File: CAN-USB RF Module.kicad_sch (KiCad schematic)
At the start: 27 parts, among them J1 Conn_01x05_Pin, J2 USB_B_Micro, J3 Conn_Coaxial, SW1 RESET, SW2 BOOT0, U1 STM32L562CETx, U2 TLV2217-33KVURG3, U3 AT86RF215-ZU, U4 MCP2542WFDxMF, Y1 8 MHz

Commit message: Added most parts still have to pick better power regulator
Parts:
- removed C3, C4: 100n, symbol Device:C
- removed J1: Conn_01x05_Pin, Connector_PinHeader_2.54mm:PinHeader_1x05_P2.54mm_Vertical, symbol Connector:Conn_01x05_Pin
- removed U1: STM32L562CETx, Package_QFP:LQFP-48_7x7mm_P0.5mm, symbol MCU_ST_STM32L5:STM32L562CETx
- removed U3: AT86RF215-ZU, footprints:QFN48_7X7_PQ_MCH, symbol 2023-05-29_04-56-52:AT86RF215-ZU
- added C14: 100n, Capacitor_SMD:C_0402_1005Metric, symbol Device:C
- added C15: 100u, Capacitor_SMD:C_0402_1005Metric, symbol Device:C
- added CR1: ESDCAN03-2BWY, SOT323-3L_STM, symbol RF_Parts:ESDCAN03-2BWY
- added D2: USBLC6-2SC6, digikey-footprints:SOT23-6L, symbol dk_TVS-Diodes:USBLC6-2SC6
- added D3: ESDA7P120-1U1M, ESDA8P801U1M, symbol RF_Parts:ESDA7P120-1U1M
- added D4: SMLVT3V3, DIOM5436X265N, symbol RF_Parts:SMLVT3V3
- added IC1: ESDALC6V1W5, SOT65P210X110-5N, symbol RF_Parts:ESDALC6V1W5
- added J1, J4: Conn_01x06_Pin, Connector_PinHeader_2.54mm:PinHeader_1x06_P2.54mm_Vertical, symbol Connector:Conn_01x06_Pin
- added R3: 390, Resistor_SMD:R_0402_1005Metric, symbol Device:R
- added U1: STM32L442KCUx, Package_DFN_QFN:QFN-32-1EP_5x5mm_P0.5mm_EP3.45x3.45mm, symbol MCU_ST_STM32L4:STM32L442KCUx
- added U3: SX1280IMLTRT, QFN24_4X4_SEM, symbol RF_Parts:SX1280IMLTRT
- C1, C10, C11, C2, C7, C8: footprint (none) -> Capacitor_SMD:C_0402_1005Metric
- C12, C13: value 100n -> 14p; footprint (none) -> Capacitor_SMD:C_0402_1005Metric
- C5, C6, C9: footprint (none) -> Capacitor_SMD:C_0603_1608Metric
- D1: footprint (none) -> LED_SMD:LED_0402_1005Metric
- FB1: footprint (none) -> Resistor_SMD:R_0603_1608Metric
- J2: footprint Connector_USB:USB_Micro-B_Amphenol_10104110_Horizontal -> footprints:1981568-1
- R1: footprint (none) -> Resistor_SMD:R_0402_1005Metric
- R2: footprint (none) -> Resistor_SMD:R_0805_2012Metric
- SW1: footprint (none) -> footprints:SMD_025816_WRE
- SW2: footprint (none) -> Button_Switch_SMD:SW_SPDT_PCM12
- U2: footprint footprints:KVU3_TEX -> KVU3_TEX; symbol 2023-05-29_05-41-45:TLV2217-33KVURG3 -> RF_Parts:TLV2217-33KVURG3
- U4: value MCP2542WFDxMF -> MCP2542WFDxMF (CAN)
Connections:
- net +3.3V: now also U4.3 (VDD), C15.2, D4.1 (K), J4.1 (Pin_1), U1.1 (VDD), U1.17 (VDD)
- net +3.3VA: now also U1.5 (VDDA)
- net BOOT0: now also U1.31 (PH3)
- net GND: now also U4.2 (VSS), U4.9 (VSS), C14.1, C15.1, CR1.3, D2.2, D3.2 (A), D4.2 (A), IC1.2 (GND), J1.6 (Pin_6), J4.3 (Pin_3), U1.16 (VSS), U1.32 (VSS), U1.33 (VSS)
- net NRST: now also IC1.1 (I/01), J4.5 (Pin_5), U1.4 (NRST)
- net RCC_OSC_OUT: now also R3.2; no longer C12.1, Y1.4
- net VBUS: now also J2.4 (ID), C14.2, D2.5, D3.1 (K)
- net USART2_CANTX: now reaches U4.1 (TXD)
- net USART2_CANTX: now also U1.20 (PA10)
- net USART2_CANRX: now reaches U4.4 (RXD)
- net USART2_CANRX: now also U1.19 (PA9)
- net at U4.6 (CANL): now also CR1.1, J1.4 (Pin_4)
- net at U4.7 (CANH): now also CR1.2, J1.2 (Pin_2)
- net USART2_CANSTBY: now reaches U4.8 (STBY)
- net USART2_CANSTBY: now also U1.18 (PA8)
- net USB_D-_C: now reaches J2.2 (D-)
- net USB_D-_C: now also D2.1
- net USB_D+_C: now reaches J2.3 (D+)
- net USB_D+_C: now also D2.3
- new net: C12.1, R3.1, Y1.4
- new net DEBUG_JTDO-SWO: IC1.3 (I/02), J4.6 (Pin_6)
- new net DEBUG_JTSK_SWCLK: IC1.5 (I/04), J4.2 (Pin_2), U1.24 (PA14)
- new net DEBUG_JTSK_SWDIO: IC1.4 (I/03), J4.4 (Pin_4), U1.23 (PA13)
- new net DEBUG_JTSK_SWO: U1.26 (PB3)
- new net USB_D+: D2.4, U1.22 (PA12)
- new net USB_D-: D2.6, U1.21 (PA11)
- no-connect marks 0 -> 21
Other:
- note added: "(CL - CS) * 2 = C1,2 = (12p - 5p) * 2 = 14p"
- note added: "8MHz External Crystal HSE"
- note added: "ESD Protected CAN Tranciever"
- note added: "ESD Protected USB"
- note added: "STLINK Debug Connector with ESD Protection"
- note added: "STM32L442KCUx"
- note added: "USB Power 5v and CAN Power 12v to 3v3 With ESD Protection"
- note removed: "STM32L562CET6"
- note removed: "USB Power 5v and CAN Power 12v to 3v3"
- moved on the sheet: C1, C10, C11, C12, C13, C2, C5, C6, C7, C8, D1, FB1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

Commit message: l
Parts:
- added H1, H2, H4: MountingHole, symbol Mechanical:MountingHole
- added H3: MountingHole, MountingHole:MountingHole_2.2mm_M2_DIN965, symbol Mechanical:MountingHole
- added U5: MCP2517FD-xSL, Package_SO:SOIC-14_3.9x8.7mm_P1.27mm, symbol Interface_CAN_LIN:MCP2517FD-xSL
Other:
- note added: "Talks over UART not SPI"
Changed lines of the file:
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@@
     (effects (font (size 1.27 1.27)) (justify left bottom))
   )
-  (text "Final parts bill:\n\nLDO Voltage Regulator : https://www.digikey.ca/en/products/detail/texas-instruments/TLV2217-33KVURG3/1096010\n\nSTM32L562CET6 : https://www.st.com/en/microcontrollers-microprocessors/stm32l562ce.html#sample-buy\n\nRF Tranciever AT86RF215-ZU : https://www.digikey.ca/en/products/detail/microchip-technology/AT86RF215-ZU/5147177\n\nCAN Tranciever MCP2544WFD-E/FSN : https://www.digikey.ca/en/products/detail/microchip-technology/MCP2544WFD-E%2FSN/5975771\n\n8 MHz Crystal Occilator ECS-80-12-33-JGN-TR : https://www.digikey.ca/en/products/detail/ecs-inc/ECS-80-12-33-JGN-TR/10478754\n\nUSB ESD PROTECTION TVS : https://www.digikey.ca/en/products/detail/stmicroelectronics/USBLC6-2SC6/1040559\n\nSWD ESD PROTECTION IC : https://www.digikey.ca/en/products/detail/stmicroelectronics/ESDALC6V1W5/1037997\n\nSWD ESD PROTECTION DIODE : https://www.digikey.ca/en/products/detail/stmicroelectronics/SMLVT3V3/603521\n\nPOWER DIODE ESDA7P120-1U1M : https://www.digikey.ca/en/products/detail/stmicroelectronics/ESDA7P120-1U1M/6709858\n\nCAN Transciever ESD Protection ESDCAN03-2BWY : https://www.digikey.ca/en/products/detail/stmicroelectronics/ESDCAN03-2BWY/5305266\n\nButton Push : https://www.digikey.ca/en/products/detail/w%C3%BCrth-elektronik/434133025816/9950810\n\n"
-    (at 444.5 77.47 0)
+  (text "Final parts bill:\n\nLDO Voltage Regulator : https://www.digikey.ca/en/products/detail/texas-instruments/TLV2217-33KVURG3/1096010\n\nSTM32L562CET6 : https://www.st.com/en/microcontrollers-microprocessors/stm32l562ce.html#sample-buy\n\nRF Tranciever AT86RF215-ZU : https://www.digikey.ca/en/products/detail/microchip-technology/AT86RF215-ZU/5147177\n\nCAN Tranciever MCP2544WFD-E/FSN : https://www.digikey.ca/en/products/detail/microchip-technology/MCP2544WFD-E%2FSN/5975771\n\n8 MHz Crystal Occilator ECS-80-12-33-JGN-TR : https://www.digikey.ca/en/products/detail/ecs-inc/ECS-80-12-33-JGN-TR/10478754\n\nUSB ESD PROTECTION TVS : https://www.digikey.ca/en/products/detail/stmicroelectronics/USBLC6-2SC6/1040559\n\nSWD ESD PROTECTION IC : https://www.digikey.ca/en/products/detail/stmicroelectronics/ESDALC6V1W5/1037997\n\nSWD ESD PROTECTION DIODE : https://www.digikey.ca/en/products/detail/stmicroelectronics/SMLVT3V3/603521\n\nPOWER DIODE ESDA7P120-1U1M : https://www.digikey.ca/en/products/detail/stmicroelectronics/ESDA7P120-1U1M/6709858\n\nCAN Transciever ESD Protection ESDCAN03-2BWY : https://www.digikey.ca/en/products/detail/stmicroelectronics/ESDCAN03-2BWY/5305266\n\nButton Push : https://www.digikey.ca/en/products/detail/w%C3%BCrth-elektronik/434133025816/9950810\n\nCAN 2.0 Controller MCP2517FD-H/FSL : https://www.digikey.ca/en/products/detail/microchip-technology/MCP2517FD-H%2FSL/7691348?"
+    (at 444.5 86.36 0)
     (effects (font (size 1.27 1.27)) (justify left bottom))
   )
@@
   )
   (text "ESD Protected CAN Tranciever\n" (at 289.56 236.855 0)
+    (effects (font (size 1.27 1.27)) (justify left bottom))
+  )
+  (text "Talks over UART not SPI\n" (at 33.02 146.05 0)
     (effects (font (size 1.27 1.27)) (justify left bottom))
   )
@@
         (path "/05ffaa46-4df3-4c93-a015-882eb69d3f55"
           (reference "C7") (unit 1)
+        )
+      )
+    )
+  )
+  (symbol (lib_id "Mechanical:MountingHole") (at 32.385 81.28 0) (unit 1)
+    (in_bom yes) (on_board yes) (dnp no) (fields_autoplaced)
+    (property "Reference" "H1" (at 35.56 80.645 0)
+      (effects (font (size 1.27 1.27)) (justify left))
+    )
+    (property "Value" "MountingHole" (at 35.56 83.185 0)
+      (effects (font (size 1.27 1.27)) (justify left))
+    )
+    (property "Footprint" "" (at 32.385 81.28 0)
+      (effects (font (size 1.27 1.27)) hide)
+    )
+    (property "Datasheet" "~" (at 32.385 81.28 0)
+      (effects (font (size 1.27 1.27)) hide)
+    )
+    (instances
+      (project "CAN-USB RF Module"
+        (path "/05ffaa46-4df3-4c93-a015-882eb69d3f55"
+          (reference "H1") (unit 1)
         )
       )
@@
     )
   )
+  (symbol (lib_id "Mechanical:MountingHole") (at 41.91 81.28 0) (unit 1)
+    (in_bom yes) (on_board yes) (dnp no) (fields_autoplaced)
+    (property "Reference" "H2" (at 45.085 80.645 0)
+      (effects (font (size 1.27 1.27)) (justify left))
+    )
+    (property "Value" "MountingHole" (at 45.085 83.185 0)
+      (effects (font (size 1.27 1.27)) (justify left))
+    )
+    (property "Footprint" "" (at 41.91 81.28 0)
+      (effects (font (size 1.27 1.27)) hide)
+    )
+    (property "Datasheet" "~" (at 41.91 81.28 0)
+      (effects (font (size 1.27 1.27)) hide)
+    )
+    (instances
+      (project "CAN-USB RF Module"
+        (path "/05ffaa46-4df3-4c93-a015-882eb69d3f55"
+          (reference "H2") (unit 1)
+        )
+      )
+    )
+  )
   (symbol (lib_id "power:GND") (at 469.265 117.475 0) (unit 1)
     (in_bom yes) (on_board yes) (dnp no) (fields_autoplaced)
@@
     )
   )
+  (symbol (lib_id "Mechanical:MountingHole") (at 51.435 81.915 0) (unit 1)
+    (in_bom yes) (on_board yes) (dnp no) (fields_autoplaced)
+    (property "Reference" "H3" (at 54.61 81.28 0)
+      (effects (font (size 1.27 1.27)) (justify left))
+    )
+    (property "Value" "MountingHole" (at 54.61 83.82 0)
+      (effects (font (size 1.27 1.27)) (justify left))
+    )
+    (property "Footprint" "MountingHole:MountingHole_2.2mm_M2_DIN965" (at 51.435 81.915 0)
+      (effects (font (size 1.27 1.27)) hide)
+    )
+    (property "Datasheet" "~" (at 51.435 81.915 0)
+      (effects (font (size 1.27 1.27)) hide)
+    )
+    (instances
+      (project "CAN-USB RF Module"
+        (path "/05ffaa46-4df3-4c93-a015-882eb69d3f55"
+          (reference "H3") (unit 1)
+        )
+      )
+    )
+  )
   (symbol (lib_id "Device:C") (at 194.945 36.195 0) (unit 1)
     (in_bom yes) (on_board yes) (dnp no)
@@
         (path "/05ffaa46-4df3-4c93-a015-882eb69d3f55"
           (reference "C5") (unit 1)
+        )
+      )
+    )
+  )
+  (symbol (lib_id "Mechanical:MountingHole") (at 61.595 81.915 0) (unit 1)
+    (in_bom yes) (on_board yes) (dnp no) (fields_autoplaced)
+    (property "Reference" "H4" (at 64.77 81.28 0)
+      (effects (font (size 1.27 1.27)) (justify left))
+    )
+    (property "Value" "MountingHole" (at 64.77 83.82 0)
+      (effects (font (size 1.27 1.27)) (justify left))
+    )
+    (property "Footprint" "" (at 61.595 81.915 0)
+      (effects (font (size 1.27 1.27)) hide)
+    )
+    (property "Datasheet" "~" (at 61.595 81.915 0)
+      (effects (font (size 1.27 1.27)) hide)
+    )
+    (instances
+      (project "CAN-USB RF Module"
+        (path "/05ffaa46-4df3-4c93-a015-882eb69d3f55"
+          (reference "H4") (unit 1)
         )
       )
@@
         )
       )
+    )
+  )
+  (symbol (lib_id "Interface_CAN_LIN:MCP2517FD-xSL") (at 367.665 217.805 0) (unit 1)
+    (in_bom yes) (on_board yes) (dnp no) (fields_autoplaced)
+    (property "Reference" "U5" (at 369.6209 203.835 0)
+      (effects (font (size 1.27 1.27)) (justify left))
+    )
+    (property "Value" "MCP2517FD-xSL" (at 369.6209 206.375 0)
+      (effects (font (size 1.27 1.27)) (justify left))
+    )
+    (property "Footprint" "Package_SO:SOIC-14_3.9x8.7mm_P1.27mm" (at 367.665 243.205 0)
+      (effects (font (size 1.27 1.27)) hide)
+    )
+    (property "Datasheet" "https://ww1.microchip.com/downloads/en/DeviceDoc/20005688A.pdf" (at 367.665 211.455 0)
+      (effects (font (size 1.27 1.27)) hide)
+    )
+    (pin "1")
+    (pin "10")
+    (pin "11")
+    (pin "12")
+    (pin "13")
+    (pin "14")
+    (pin "2")
+    (pin "3")
+    (pin "4")
+    (pin "5")
+    (pin "6")
+    (pin "7")
+    (pin "8")
+    (pin "9")
+    (instances
+      (project "CAN-USB RF Module"
+        (path "/05ffaa46-4df3-4c93-a015-882eb69d3f55"
+          (reference "U5") (unit 1)
+        )
+      )

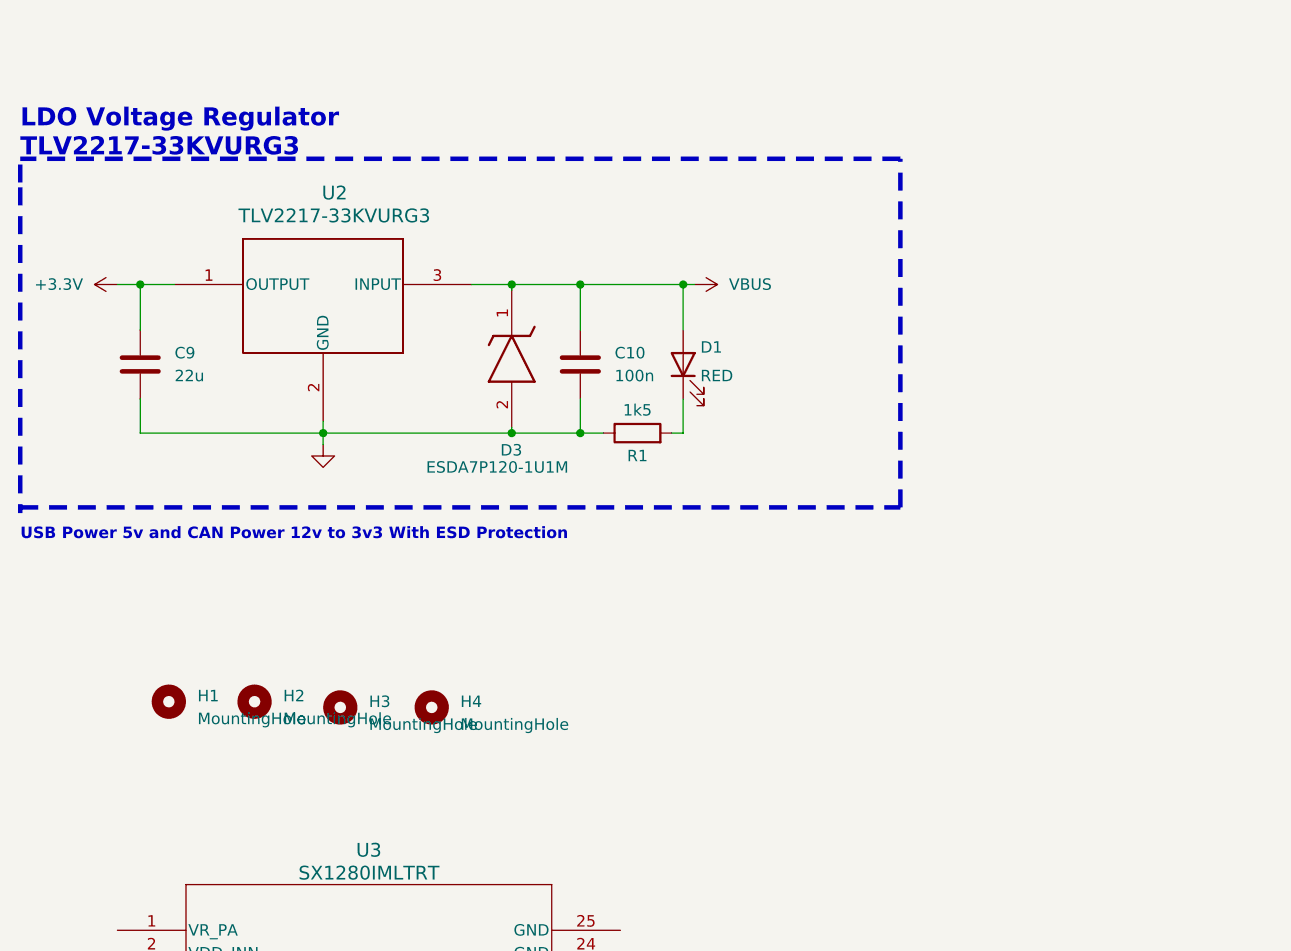
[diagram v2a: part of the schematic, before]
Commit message: Added Sheet for power regulator
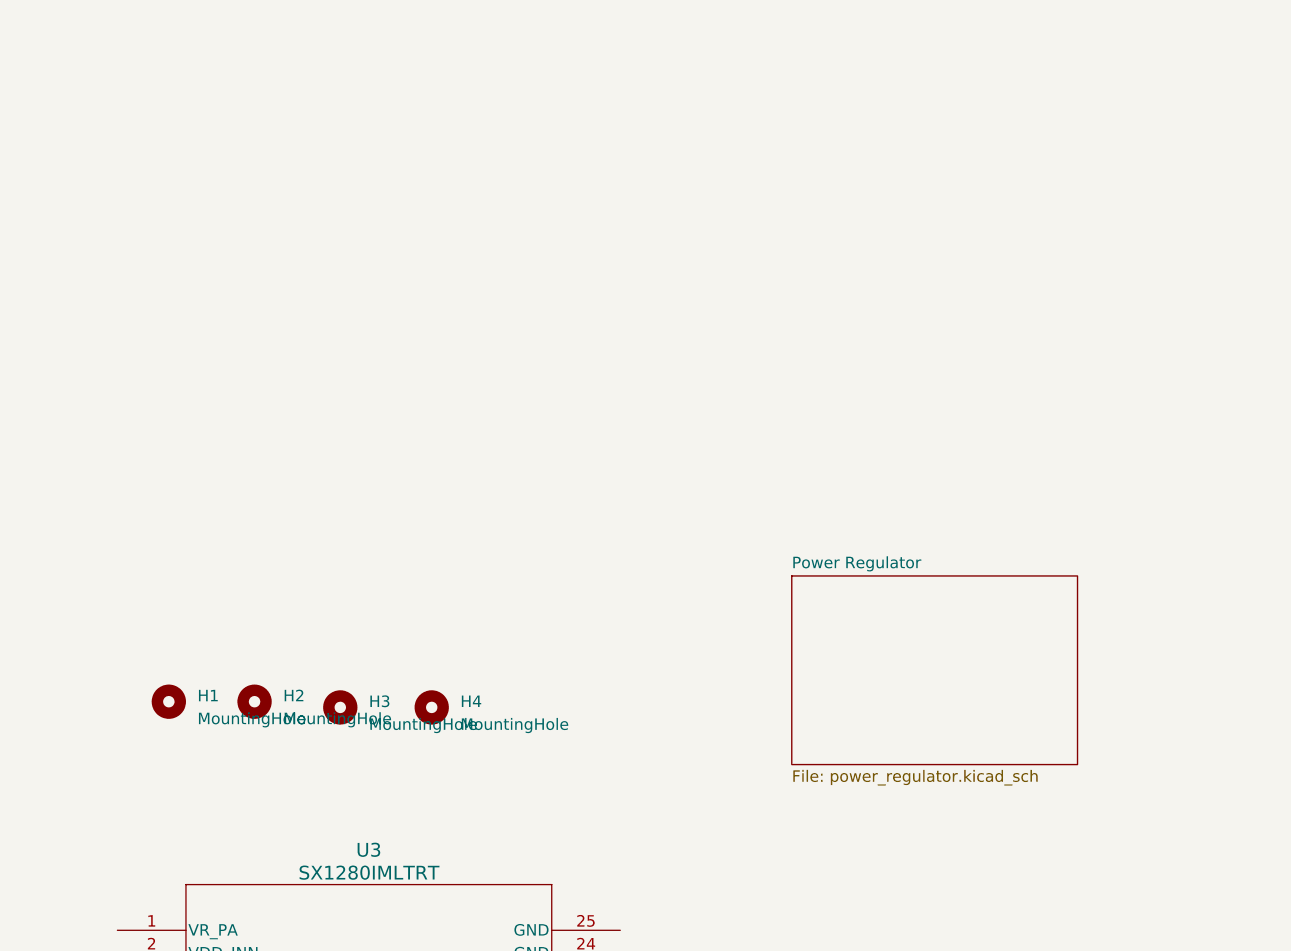
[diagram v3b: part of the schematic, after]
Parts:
- removed C10: 100n, Capacitor_SMD:C_0402_1005Metric, symbol Device:C
- removed C9: 22u, Capacitor_SMD:C_0603_1608Metric, symbol Device:C
- removed D1: RED, LED_SMD:LED_0402_1005Metric, symbol Device:LED
- removed D3: ESDA7P120-1U1M, ESDA8P801U1M, symbol RF_Parts:ESDA7P120-1U1M
- removed R1: 1k5, Resistor_SMD:R_0402_1005Metric, symbol Device:R
- removed U2: TLV2217-33KVURG3, KVU3_TEX, symbol RF_Parts:TLV2217-33KVURG3
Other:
- added sheet Power Regulator (power_regulator.kicad_sch)
- note removed: "LDO Voltage Regulator TLV2217-33KVURG3"
- note removed: "USB Power 5v and CAN Power 12v to 3v3 With ESD Protection"

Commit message: started on rf tranciever
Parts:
- removed C12, C13: 14p, Capacitor_SMD:C_0402_1005Metric, symbol Device:C
- removed C14: 100n, Capacitor_SMD:C_0402_1005Metric, symbol Device:C
- removed C15: 100u, Capacitor_SMD:C_0402_1005Metric, symbol Device:C
- removed CR1: ESDCAN03-2BWY, SOT323-3L_STM, symbol RF_Parts:ESDCAN03-2BWY
- removed D2: USBLC6-2SC6, digikey-footprints:SOT23-6L, symbol dk_TVS-Diodes:USBLC6-2SC6
- removed H1, H2, H4: MountingHole, symbol Mechanical:MountingHole
- removed H3: MountingHole, MountingHole:MountingHole_2.2mm_M2_DIN965, symbol Mechanical:MountingHole
- removed J1: Conn_01x06_Pin, Connector_PinHeader_2.54mm:PinHeader_1x06_P2.54mm_Vertical, symbol Connector:Conn_01x06_Pin
- removed J2: USB_B_Micro, footprints:1981568-1, symbol Connector:USB_B_Micro
- removed J3: Conn_Coaxial, footprints:TAOGLAS_EMPCB.SMAFSTJ.B.HT, symbol Connector:Conn_Coaxial
- removed R3: 390, Resistor_SMD:R_0402_1005Metric, symbol Device:R
- removed U1: STM32L442KCUx, Package_DFN_QFN:QFN-32-1EP_5x5mm_P0.5mm_EP3.45x3.45mm, symbol MCU_ST_STM32L4:STM32L442KCUx
- removed U3: SX1280IMLTRT, QFN24_4X4_SEM, symbol RF_Parts:SX1280IMLTRT
- removed U4: MCP2542WFDxMF (CAN), Package_DFN_QFN:DFN-8-1EP_3x3mm_P0.65mm_EP1.55x2.4mm, symbol Interface_CAN_LIN:MCP2542WFDxMF
- removed U5: MCP2517FD-xSL, Package_SO:SOIC-14_3.9x8.7mm_P1.27mm, symbol Interface_CAN_LIN:MCP2517FD-xSL
- removed Y1: 8 MHz, footprints:XTAL_ECS-240-8-33-AGN-TR, symbol Device:Crystal_GND23
- added U6: STM32L442KCU6, Package_DFN_QFN:QFN-32-1EP_5x5mm_P0.5mm_EP3.45x3.45mm, symbol MCU_ST_STM32L4:STM32L442KCUx
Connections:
- net DEBUG_JTDO-SWO is gone; now on net DEBUG_JTSK_SWO: IC1.3 (I/02), J4.6 (Pin_6)
- net +3.3V: now also U6.1 (VDD), U6.17 (VDD)
- net +3.3VA: now also U6.5 (VDDA)
- net BOOT0: now also U6.31 (PH3)
- net DEBUG_JTSK_SWCLK: now also U6.24 (PA14)
- net DEBUG_JTSK_SWDIO: now also U6.23 (PA13)
- net DEBUG_JTSK_SWO: now also U6.26 (PB3)
- net GND: now also U6.16 (VSS), U6.32 (VSS), U6.33 (VSS)
- net NRST: now also U6.4 (NRST)
- new net CAN_RX: U6.21 (PA11)
- new net CAN_STBY: U6.14 (PB0)
- new net CAN_TX: U6.22 (PA12)
- new net SPI1_MISO: U6.12 (PA6)
- new net SPI1_MOSI: U6.13 (PA7)
- new net SPI1_NSS: U6.10 (PA4)
- new net SPI1_SCK: U6.11 (PA5)
- new net UART1_USB_RX: U6.30 (PB7)
- new net UART1_USB_TX: U6.29 (PB6)
- no-connect marks 21 -> 13
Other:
- added sheet CAN Tranciever (CAN_Tranciever.kicad_sch)
- added sheet LoRa Tranciever (LoRa_Tranciever_sch.kicad_sch)
- added sheet USB Interface (usb_interface.kicad_sch)
- note added: "Dont have a VBUS out put rename it to +5V"
- note removed: "(CL - CS) * 2 = C1,2 = (12p - 5p) * 2 = 14p"
- note removed: "8MHz External Crystal HSE"
- note removed: "ESD Protected CAN Tranciever"
- note removed: "ESD Protected USB"
- note removed: "Talks over UART not SPI"
- moved on the sheet: C1, C11, C2, C5, C6, C7, C8, D4, FB1, IC1, J4, R2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

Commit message: Made minor changes
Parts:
- D4: footprint DIOM5436X265N -> footprints:DIOM5436X265N
- IC1: footprint SOT65P210X110-5N -> footprints:SOT65P210X110-5N
- R2: footprint Resistor_SMD:R_0805_2012Metric -> Resistor_SMD:R_0402_1005Metric
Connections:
- net DEBUG_JTSK_SWO is gone; now on net +3V3: IC1.3 (I/02), J4.6 (Pin_6), U6.26 (PB3)
- net CAN_STBY: no longer U6.14 (PB0)
- net +3.3V renamed +3V3
- no-connect marks 13 -> 14
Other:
- sheet LoRa Tranciever ports: added BUSY, DIO1, DIO2, DIO3, SX1280_NRESET; removed none
- moved on the sheet: C11, C5, D4, IC1, J4

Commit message: Done power
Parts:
- D1: renamed from D4; JLC # (none) -> C283619
- IC1: JLC # (none) -> C5116446
- U1: renamed from U6; JLC # (none) -> C2969865
- renumbered C11 to C1, C5 to C2, C2 to C3, C1 to C4, C8 to C5, J4 to J1, R2 to R1
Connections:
- net CAN_STBY: now also U1.3 (PC15)
- net UART1_USB_RX: no longer U1.30 (PB7)
- net UART1_USB_TX: no longer U1.29 (PB6)
- net DIO0: now reaches U1.14 (PB0)
- net DIO1: now reaches U1.15 (PB1)
- net SW_RXTX: now reaches U1.27 (PB4)
- net SX_RESET: now reaches U1.28 (PB5)
- net UART2_USB_CTS: now reaches U1.6 (PA0)
- net UART2_USB_RTS: now reaches U1.7 (PA1)
- net UART2_USB_TX: now reaches U1.8 (PA2)
- net UART2_USB_RX: now reaches U1.9 (PA3)
- new net DIO2: U1.29 (PB6)
- new net DIO3: U1.30 (PB7)
- no-connect marks 14 -> 5
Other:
- sheet LoRa Tranciever ports: added DIO0, MISO_TX, RXTX_EXT, SX1276_NRESET; removed BUSY, MOSI_TX, SX1280_NRESET
- sheet USB Interface ports: added CTS, RESET, RTS; removed none
- note added: "@Note The NRST is wired to the usb interface aswell as a button and both can reset"
- note added: "Power In - Blue Fault - Red Status - Green TX/RX - Amber"
- note added: "STLINK Debug Connector with ESD Protection JTAG ESD Protection"
- note added: "STM32L442KCU6 MCU"
- note added: "We can use usb to program and reset the mcu"
- note removed: "STLINK Debug Connector with ESD Protection"
- note removed: "STM32L442KCUx"
- moved on the sheet: C1, SW1
